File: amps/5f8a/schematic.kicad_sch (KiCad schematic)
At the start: 74 parts, among them T3 45268

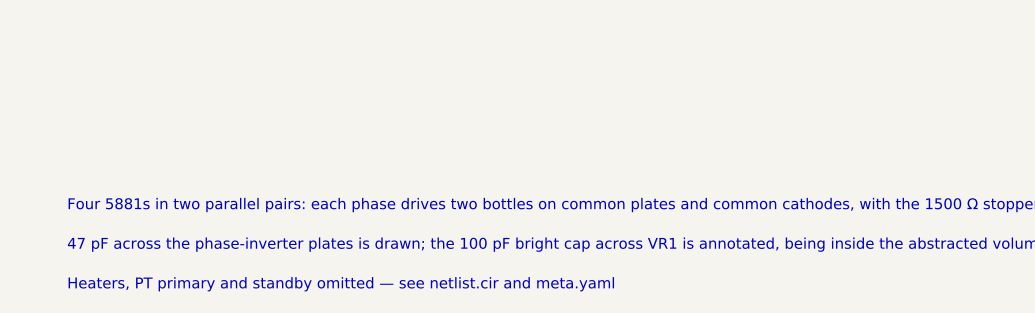
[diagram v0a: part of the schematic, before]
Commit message: Fix: schematic sheet notes no longer name repository files
Thirty-seven committed sheets rendered footnotes and section notes such as
"Heaters and PT primary omitted — see netlist.cir and meta.yaml" or
"excluded from netlist.cir (notes.md)" to visitors through KiCanvas. The
prose sweeps never counted sheets. Rewritten in the site's own words — the
netlist, the sources list, the circuit story, the parts list, the board
drawing — in 59 strings across 33 draw scripts, keeping every technical
claim as it was; the three tone sheets (6G4, 6G5, 6G6-B) are under repair
elsewhere and keep theirs for now. The sweep touched only strings passed to
the sheet's note, text, caption and footnote calls, never a path or a value.

Gates: check_schematics 40/0, connectivity 0 isolated pins;
verify_schematic_nets 40 clean; only the regenerated sheets and their served
copies changed.

Co-Authored-By: Claude Fable 5.1 <noreply@anthropic.com>
Claude-Session: https://claude.ai/code/session_01KBMfdh37HmCL2iWcBiL5J1
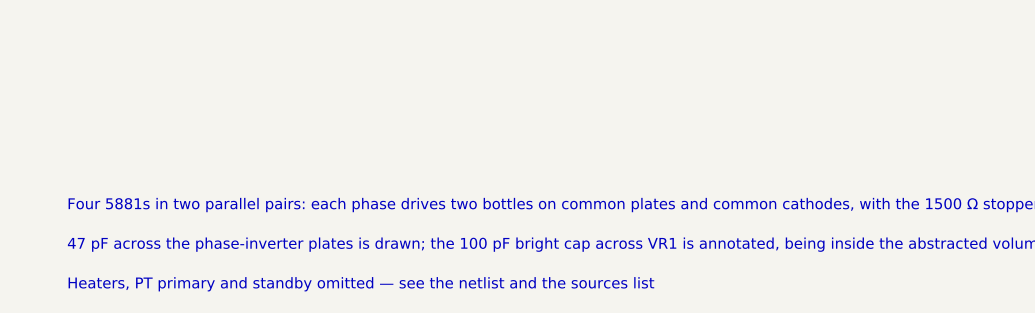
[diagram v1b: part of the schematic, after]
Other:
- note added: "Heaters, PT primary and standby omitted — see the netlist and the sources list"
- note removed: "Heaters, PT primary and standby omitted — see netlist.cir and meta.yaml"
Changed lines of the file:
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@@
   (text "47 pF across the phase-inverter plates is drawn; the 100 pF bright cap across VR1 is annotated, being inside the abstracted volume network" (at 12.7 200.68 0)
     (effects (font (size 1.2 1.2)) (justify left)))
-  (text "Heaters, PT primary and standby omitted — see netlist.cir and meta.yaml" (at 12.7 205.08 0)
+  (text "Heaters, PT primary and standby omitted — see the netlist and the sources list" (at 12.7 205.08 0)
     (effects (font (size 1.2 1.2)) (justify left)))
   (sheet_instances (path "/" (page "1")))

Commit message: Fix: state the datasheet unit on 17 dual-triode sections whose sheets printed the other half's pin numbers
The sheet-vs-board gate reported these sockets as SECTION-SWAP; the
2026-09-10 source-read triage found the BOARD right on every one of them
(and both surfaces wrong on the 5G9 tremolo bottle). Each sheet had
lettered the section on the default map (A -> unit 1 -> pins 6/7/8) where
the factory drawing puts that stage on 1/2/3. The draw scripts now state
`unit=` on both halves, with the source cited beside the call, so the
printed socket numbers are the factory's:

- 5f4 V3: driver V3A -> 1/2/3, cathodyne V3B -> 6/7/8
  (crop 5f4-V3-layout-trace.png: +213 V driver plate -> pin 1, +270 V -> 6)
- 5f8a V3: 82k half V3A -> 1/2/3, 100k half V3B -> 6/7/8
  (crop 5f8a-V3-layout-trace.png: +225 -> 6, +19 -> 2, +28.5 -> 8)
- 6161 V1: channel 1 V1A -> 1/2/3 (crop 6161-V1-ch1.png prints 1/2/3);
  6161 V2: 1 MEG-grid half V2A -> 1/2/3, paraphase V2B -> 6/7/8
  (crop 6161-V2.png / 6161-V2-right.png)
- 6g3 V3: 82k half V3A -> 1/2/3 (crop 6g3-V3-layout-wires.png: +230 -> 1,
  +225 -> 6, +20 -> 7)
- aa1164 V3: recovery V3A -> 1/2/3, mixer V3B -> 6/7/8
  (crops aa1164-V3A-recovery-schem.png, aa1164-V3B-mixer-schem.png)
- aa864-bassman V1/V2: input stages 2/1/3, second stages 7/6/8; V4: the
  .1/500 pF-fed 82k half 2/1/3 (crops aa864-V1A-input.png,
  aa864-V1B-second.png, aa864-V2A-input.png, aa864-V2B-second.png,
  aa864-V4-PI.png)
- ab165 V1/V2/V4: same pattern (crops ab165-V1A-input.png,
  ab165-V1B-second.png, ab165-V2A-input.png, ab165-V2B-second.png,
  ab165-V4-PI.png)
- ab763-super V1/V2: slope-plate +270 V -> pin 1 (input stage), .047
  plate -> 6 (crops ab763-super-V1-layout-sh.png, ab763-super-V2-layout-sh.png)
- dr103 V2/V3: gain stages 6/7/8, cathode followers 1/2/3 (crops
  dr103-V2-huss.png, dr103-V3-huss.png — the Huss redraw, not a factory
  print; noted in the script)
- 5g9 V3: oscillator V3A -> 1/2/3, follower V3B -> 6/7/8 (crops
  5g9-V3-strap71-zoom.png, 5g9-V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
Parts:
- V3A: Basing_unit (none) -> 2
- V3B: Basing_unit (none) -> 1
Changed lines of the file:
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@@
     (in_bom yes) (on_board yes)
     (property "Reference" "V3A" (at 189.866 57.1016 0) (effects (font (size 1.27 1.27)) (justify left)))
-    (property "Value" "12AX7" (at 189.866 59.5016 0) (effects (font (size 1.27 1.27)) (justify left))))
+    (property "Value" "12AX7" (at 189.866 59.5016 0) (effects (font (size 1.27 1.27)) (justify left)))
+    (property "Basing_unit" "2" (at 189.866 61.9016 0) (effects (font (size 1.27 1.27)) hide)))
   (wire (pts (xy 176.246 63.5016) (xy 176.246 63.5016))
     (stroke (width 0) (type default)))
@@
     (in_bom yes) (on_board yes)
     (property "Reference" "V3B" (at 171.961 97.7816 0) (effects (font (size 1.27 1.27)) (justify left)))
-    (property "Value" "12AX7" (at 171.961 100.182 0) (effects (font (size 1.27 1.27)) (justify left))))
+    (property "Value" "12AX7" (at 171.961 100.182 0) (effects (font (size 1.27 1.27)) (justify left)))
+    (property "Basing_unit" "1" (at 171.961 102.582 0) (effects (font (size 1.27 1.27)) hide)))
   (wire (pts (xy 183.866 55.8816) (xy 183.866 52.4016))
     (stroke (width 0) (type default)))
@@
   (text "3" (at 125.026 86.8516 0)
     (effects (font (size 1.1 1.1)) (justify left)))
-  (text "6" (at 184.716 57.1516 0)
-    (effects (font (size 1.1 1.1)) (justify left)))
-  (text "7" (at 176.919 62.1016 0)
-    (effects (font (size 1.1 1.1)) (justify left)))
-  (text "8" (at 186.166 69.8516 0)
-    (effects (font (size 1.1 1.1)) (justify left)))
-  (text "1" (at 184.716 91.1516 0)
-    (effects (font (size 1.1 1.1)) (justify left)))
-  (text "2" (at 176.919 96.1016 0)
-    (effects (font (size 1.1 1.1)) (justify left)))
-  (text "3" (at 184.716 103.852 0)
+  (text "1" (at 184.716 57.1516 0)
+    (effects (font (size 1.1 1.1)) (justify left)))
+  (text "2" (at 176.919 62.1016 0)
+    (effects (font (size 1.1 1.1)) (justify left)))
+  (text "3" (at 186.166 69.8516 0)
+    (effects (font (size 1.1 1.1)) (justify left)))
+  (text "6" (at 184.716 91.1516 0)
+    (effects (font (size 1.1 1.1)) (justify left)))
+  (text "7" (at 176.919 96.1016 0)
+    (effects (font (size 1.1 1.1)) (justify left)))
+  (text "8" (at 184.716 103.852 0)
     (effects (font (size 1.1 1.1)) (justify left)))
   (text "3" (at 248.186 30.5166 0)

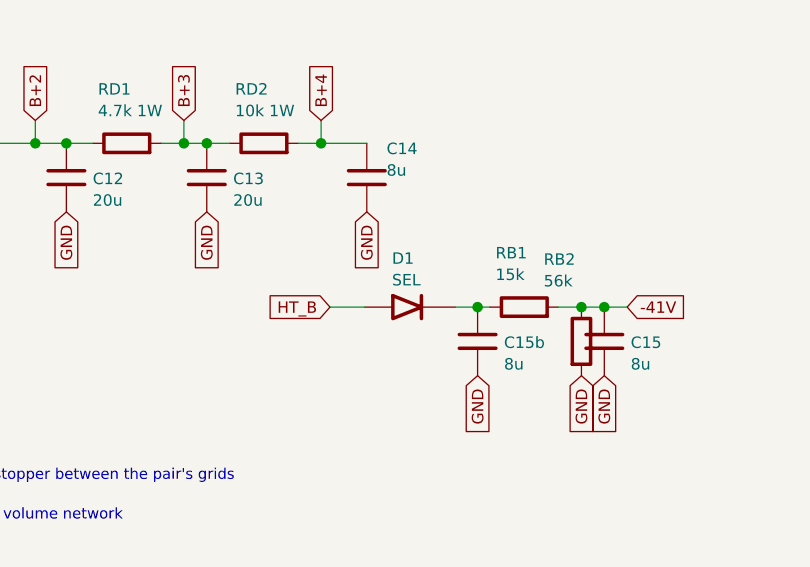
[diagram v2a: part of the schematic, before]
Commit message: Fix: 17 bias rectifiers and six HT diodes drawn backwards; the 6G6-B and 6G4 bias rows as their drawings show; AA1164 V4 units
Rectifier polarity has no gate. The netlists model every supply as an ideal
source, the sheet-vs-board check treats a two-terminal part as unordered, and
the boards' `cathode:` fields were copied from the sheets. Measured over all
68 diodes on 40 sheets: 18 negative-bias rectifiers had the cathode on the
negative node (a diode that way round would charge the node POSITIVE), and all
six 6G6-B HT diodes pointed away from B+. The printed negative bias on each of
those sheets falsifies the drawn orientation; the nine bias rectifiers already
right (AA1164, AA864, AB165, B15N, DR103, JTM100, M1959, M2204, 6G6-B) show
the idiom. Flipped: 5E4-A, 5E5-A, 5E6-A, 5F10, 5F4, 5F6, 5F6-A, 5F8-A, 5G9,
6G2, 6G3, 6G4, 6G5, AA964, AB763, AB763 Super, AB763 Twin, JTM45 (the
M1987's is with the Marshall board repair) and the 6G6-B's DR1-DR6. The
5F8-A board, which had copied its sheet, has the band moved to the tap side;
the other boards' bands are with the board-repair wave. A gate is next.

6G6-B bias. E-FB (6431x3364): the 1K 1W rises from TR1's SECOND secondary
terminal, a bias tap between the upper HT end and the grounded centre tap,
to the diode's + end. The sheet fed the diode from the HT end with the 1K
after it. T1 now carries its tap pin and the row reads tap -> 1K -> diode ->
-54 V. (The triage had read "HT end"; the native crop shows the tap.)

6G4 bias. A-FJ, read natively: tap -> rectifier -> 8 uF -> 10K -> the -55 V
node, which carries a second 8 uF and the 56K to ground as a bleeder. The
sheet fed the rectifier from an HT end, drew the 56K in series and carried
one capacitor. CBIAS2 joins the parts list, and RBIAS1's role now says
bleeder.

AA1164 V4. The K-FD sheet prints the phase inverter 7/6/8 and the tremolo
oscillator 2/1/3 (5554x4346); the sheet had them the other way round.

Gates: check_schematics 40/0 (+selftest), verify_schematic_nets 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
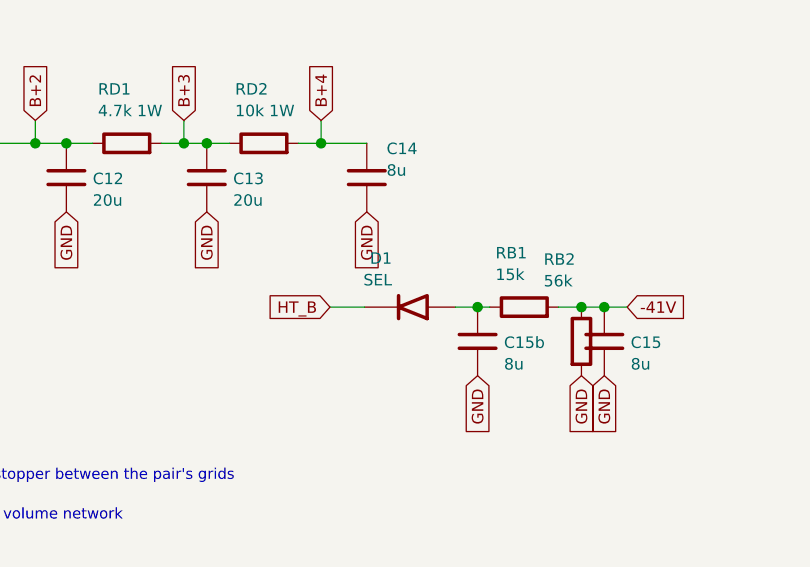
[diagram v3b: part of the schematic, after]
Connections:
- net HT_B: now also D1.2 (K); no longer D1.1 (A)
- net at C15b.1, RB1.1: now also D1.1 (A); no longer D1.2 (K)
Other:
- moved on the sheet: D1
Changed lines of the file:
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@@
   (wire (pts (xy 151.836 177.502) (xy 155.646 177.502))
     (stroke (width 0) (type default)))
-  (symbol (lib_id "cx:DIODE_SS") (at 160.726 177.502 0) (unit 1)
+  (symbol (lib_id "cx:DIODE_SS") (at 160.726 177.502 180) (unit 1)
     (in_bom yes) (on_board yes)
     (property "Reference" "D1" (at 158.726 172.102 0) (effects (font (size 1.27 1.27)) (justify left)))

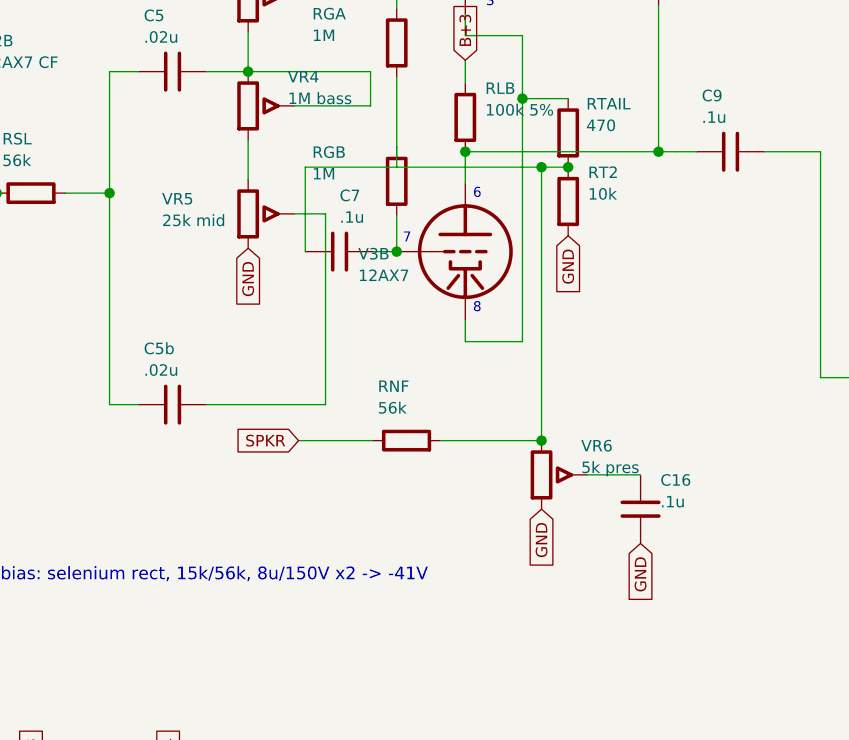
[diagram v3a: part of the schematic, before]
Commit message: Fix: 5F8-A tail foot modelled and drawn as I-EG draws it; its two printed tail figures are disputed
- The 5F6-A's fault on its sibling. I-EG schematic (6310 x 3506, crops
  (3050,480)-(3720,2320), (5300,480)-(6310,2600)): the tail's 10k runs to a
  vertical carrying the 56k from the speaker, the V3B grid's .1-200 and the 5k
  presence track (lower lug grounded). I-EG layout (6368 x 3218, crops
  (3390,1300)-(4500,2200), (2477,460)-(4175,2830)): the 10k's top eyelet, joined
  under the board to the 56k's eyelet and the presence lead, separate from the
  grounded eyelet beside it.
- Netlist: RT2 JPI PRES; RNF PRES 0 56k; RPRES PRES 0 5k; C7 GPIB PRES
  modelled. The "printed chart (J +27 V across 10k = 2.7 mA) confirms that
  reading" comment is gone.
- Sheet: RT2's foot runs down to the node; RNF, VR6 and C7 off J. sch_map
  element_pins RPRES.
- Board: it already drew the foot (RT2.b with C7.b, RNF.b, VR6.lug3); the
  net_map anchor that collapsed VR6.lug3 to ground to suit the old netlist is
  removed and RPRES declared netlist_unplaced. Caption and BOM notes: the 56k is
  a board part in the factory layout, drawn at the speaker jacks here.
- Chart: KPI 29.6 -> 41.1 V, JPI 28.2 -> 39.8 V against printed 28.5 / 27. The
  printed plates imply 2.82 mA; x 10k = 28.2 V fits only a grounded foot, so both
  are disputed with that arithmetic; PRES informational (12.5 V). Notes: the
  "tail foot" simplification (which said the chart supported a grounded foot)
  becomes its own section; 14 -> 12 gated nodes.
- sheet-board 5f8a: MISPLACED C7, RNF, RT2, VR6#ends cleared (C14 and D1
  remain; not this fix). verify_schematic_nets and verify_layout_nets 5f8a PASS
  (report-only).

Co-Authored-By: Claude Opus 5 (1M context) <noreply@anthropic.com>
Claude-Session: https://claude.ai/code/session_01KBMfdh37HmCL2iWcBiL5J1
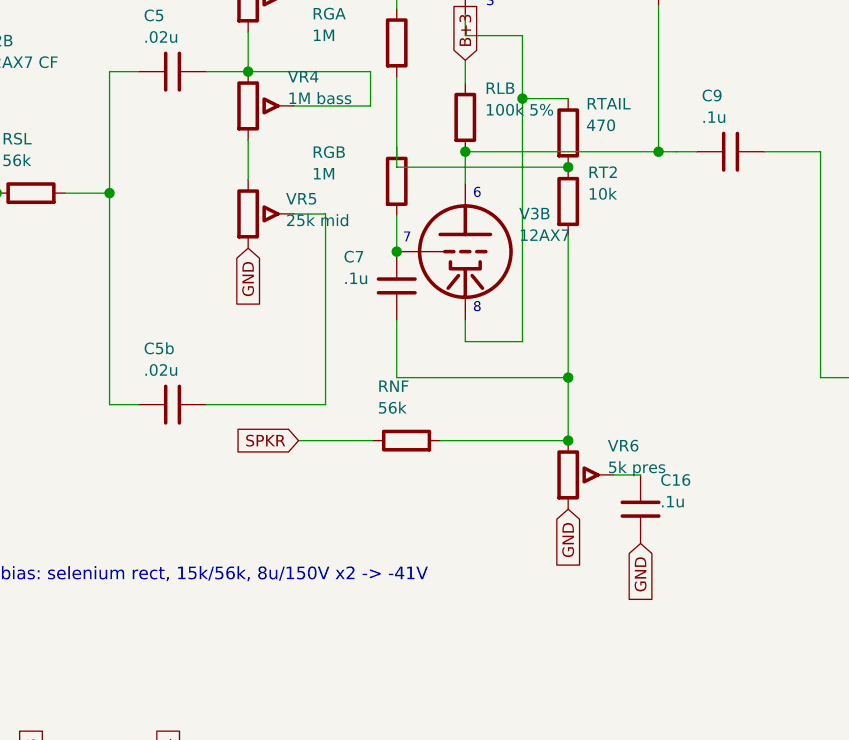
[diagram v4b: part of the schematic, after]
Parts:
- removed C11b: 20u, symbol cx:C
- removed C15: 8u, symbol cx:C
- removed C16: .1u, symbol cx:C
- added C11: 20u, symbol cx:C
- added RB2: 56k, symbol cx:R
- added VR6: 5k pres, symbol cx:POT
- C15: renamed from RB2; value 56k -> 8u; symbol cx:R -> cx:C
- C16: renamed from VR6; value 5k pres -> .1u; symbol cx:POT -> cx:C
- renumbered C11 to C11b
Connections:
- net -41V: now also RB2.1
- net B+1: now also C11.1
- net GND: now also C16.2, C11.2, RB2.2, VR6.3; no longer C16.3, RT2.2
- net at RGA.2, RGB.1, RT2.1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: no longer C16.1, C7.1, RNF.2
- net at RGB.2, V3B.2 (G): no longer C7.2
- new net: C16.1, VR6.2 (W)
- new net: C7.2, RNF.2, RT2.2, VR6.1
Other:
- moved on the sheet: C11b
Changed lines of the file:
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@@
   (symbol (lib_id "cx:POT") (at 159.736 93.3116 0) (unit 1)
     (in_bom yes) (on_board yes)
-    (property "Reference" "VR5" (at 150.164 91.6716 0) (effects (font (size 1.27 1.27)) (justify left)))
-    (property "Value" "25k mid" (at 150.164 94.0716 0) (effects (font (size 1.27 1.27)) (justify left))))
+    (property "Reference" "VR5" (at 163.938 91.6716 0) (effects (font (size 1.27 1.27)) (justify left)))
+    (property "Value" "25k mid" (at 163.938 94.0716 0) (effects (font (size 1.27 1.27)) (justify left))))
   (global_label "GND" (shape input) (at 159.736 97.1216 270)
     (effects (font (size 1.27 1.27)) (justify right)))
@@
   (symbol (lib_id "cx:TRIODE") (at 183.866 97.5016 0) (unit 1)
     (in_bom yes) (on_board yes)
-    (property "Reference" "V3B" (at 171.961 97.7816 0) (effects (font (size 1.27 1.27)) (justify left)))
-    (property "Value" "12AX7" (at 171.961 100.182 0) (effects (font (size 1.27 1.27)) (justify left)))
-    (property "Basing_unit" "1" (at 171.961 102.582 0) (effects (font (size 1.27 1.27)) hide)))
+    (property "Reference" "V3B" (at 189.846 93.3216 0) (effects (font (size 1.27 1.27)) (justify left)))
+    (property "Value" "12AX7" (at 189.846 95.7216 0) (effects (font (size 1.27 1.27)) (justify left)))
+    (property "Basing_unit" "1" (at 189.846 98.1216 0) (effects (font (size 1.27 1.27)) hide)))
   (wire (pts (xy 183.866 55.8816) (xy 183.866 52.4016))
     (stroke (width 0) (type default)))
@@
     (property "Reference" "RT2" (at 197.496 88.7316 0) (effects (font (size 1.27 1.27)) (justify left)))
     (property "Value" "10k" (at 197.496 91.1316 0) (effects (font (size 1.27 1.27)) (justify left))))
-  (global_label "GND" (shape input) (at 195.296 95.7416 270)
-    (effects (font (size 1.27 1.27)) (justify right)))
   (wire (pts (xy 176.246 63.5016) (xy 176.246 70.5016))
     (stroke (width 0) (type default)))
@@
   (wire (pts (xy 176.246 85.8816) (xy 176.246 88.1216))
     (stroke (width 0) (type default)))
-  (wire (pts (xy 176.246 88.1216) (xy 192.336 88.1216))
-    (stroke (width 0) (type default)))
-  (wire (pts (xy 192.336 88.1216) (xy 195.296 88.1216))
+  (wire (pts (xy 176.246 88.1216) (xy 195.296 88.1216))
     (stroke (width 0) (type default)))
   (wire (pts (xy 176.246 97.5016) (xy 176.246 93.5016))
@@
     (property "Reference" "RGB" (at 166.846 86.4916 0) (effects (font (size 1.27 1.27)) (justify left)))
     (property "Value" "1M" (at 166.846 88.8916 0) (effects (font (size 1.27 1.27)) (justify left))))
-  (symbol (lib_id "cx:C") (at 169.896 97.5016 90) (unit 1)
+  (symbol (lib_id "cx:C") (at 176.246 101.312 0) (unit 1)
     (in_bom yes) (on_board yes)
-    (property "Reference" "C7" (at 169.896 91.3016 270) (effects (font (size 1.27 1.27)) (justify left)))
-    (property "Value" ".1u" (at 169.896 93.7016 270) (effects (font (size 1.27 1.27)) (justify left))))
-  (wire (pts (xy 173.706 97.5016) (xy 176.246 97.5016))
+    (property "Reference" "C7" (at 170.346 98.1116 0) (effects (font (size 1.27 1.27)) (justify left)))
+    (property "Value" ".1u" (at 170.346 100.512 0) (effects (font (size 1.27 1.27)) (justify left))))
+  (wire (pts (xy 176.246 105.122) (xy 176.246 111.502))
     (stroke (width 0) (type default)))
-  (wire (pts (xy 166.086 97.5016) (xy 166.086 97.5016))
+  (wire (pts (xy 176.246 111.502) (xy 195.296 111.502))
     (stroke (width 0) (type default)))
-  (wire (pts (xy 166.086 97.5016) (xy 166.086 88.1216))
+  (wire (pts (xy 195.296 95.7416) (xy 195.296 111.502))
     (stroke (width 0) (type default)))
-  (wire (pts (xy 166.086 88.1216) (xy 176.246 88.1216))
+  (wire (pts (xy 195.296 111.502) (xy 195.296 118.502))
     (stroke (width 0) (type default)))
-  (junction (at 192.336 88.1216) (diameter 1.157) (color 0 0 0 0))
-  (wire (pts (xy 192.336 88.1216) (xy 192.336 118.502))
-    (stroke (width 0) (type default)))
-  (junction (at 192.336 118.502) (diameter 1.157) (color 0 0 0 0))
+  (junction (at 195.296 111.502) (diameter 1.157) (color 0 0 0 0))
+  (junction (at 195.296 118.502) (diameter 1.157) (color 0 0 0 0))
   (symbol (lib_id "cx:R") (at 177.336 118.502 90) (unit 1)
     (in_bom yes) (on_board yes)
     (property "Reference" "RNF" (at 174.136 112.502 270) (effects (font (size 1.27 1.27)) (justify left)))
     (property "Value" "56k" (at 174.136 114.902 270) (effects (font (size 1.27 1.27)) (justify left))))
-  (wire (pts (xy 181.146 118.502) (xy 192.336 118.502))
+  (wire (pts (xy 181.146 118.502) (xy 195.296 118.502))
     (stroke (width 0) (type default)))
   (wire (pts (xy 165.336 118.502) (xy 173.526 118.502))
@@
   (global_label "SPKR" (shape input) (at 165.336 118.502 180)
     (effects (font (size 1.27 1.27)) (justify right)))
-  (symbol (lib_id "cx:POT") (at 192.336 122.312 0) (unit 1)
+  (symbol (lib_id "cx:POT") (at 195.296 122.312 0) (unit 1)
     (in_bom yes) (on_board yes)
-    (property "Reference" "VR6" (at 196.736 119.112 0) (effects (font (size 1.27 1.27)) (justify left)))
-    (property "Value" "5k pres" (at 196.736 121.512 0) (effects (font (size 1.27 1.27)) (justify left))))
-  (global_label "GND" (shape input) (at 192.336 126.122 270)
+    (property "Reference" "VR6" (at 199.696 119.112 0) (effects (font (size 1.27 1.27)) (justify left)))
+    (property "Value" "5k pres" (at 199.696 121.512 0) (effects (font (size 1.27 1.27)) (justify left))))
+  (global_label "GND" (shape input) (at 195.296 126.122 270)
     (effects (font (size 1.27 1.27)) (justify right)))
-  (wire (pts (xy 197.416 122.312) (xy 203.336 122.312))
+  (wire (pts (xy 200.376 122.312) (xy 203.336 122.312))
     (stroke (width 0) (type default)))
   (symbol (lib_id "cx:C") (at 203.336 126.122 0) (unit 1)
